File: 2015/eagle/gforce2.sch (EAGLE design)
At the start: 20 parts, among them J1 AVR_SPI_PRG_6PTH, U1 ATMEGA328P_PDIP

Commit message: new schematic
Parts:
- added C3, C4: 22pF, SparkFun-Passives:CAPPTH
- added GO_SWITCH: M02PTH, SparkFun-Connectors:M02PTH
- added GPS: (no value), SparkFun-Connectors:M04PTH
- added I2C_1, I2C_2: (no value), SparkFun-Connectors:I2C_STANDARD
- added Q1: (no value), special:XTAL/S
- added R7: 10K, SparkFun-Passives:RESISTORPTH-1/4W
- added SPI_1, SPI_2: (no value), SparkFun-Connectors:M06SILK_FEMALE_PTH
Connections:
- new net GO: GO_SWITCH.1, R7.2, U1.PD4(XCK/T0)
- new net GPS_RX: GPS.3, U1.PD3(INT1)
- new net GPS_TX: GPS.4, U1.PD2(INT0)
- new net N$2: C3.1, Q1.1, U1.PB6(XTAL1/TOSC1)
- new net N$8: C4.1, Q1.2, U1.PB7(XTAL2/TOSC2)
- net GND: now also C3.2, C4.2, GPS.2, I2C_1.1, I2C_2.1, R7.1, SPI_1.1, SPI_2.1
- net MISO: now also SPI_1.4, SPI_2.4
- net MOSI: now also SPI_1.3, SPI_2.3
- net RX: now also U1.PD0(RXD)
- net SCK: now also SPI_1.5, SPI_2.5
- net SCL: now also I2C_1.4, I2C_2.4
- net SDA: now also I2C_1.3, I2C_2.3
- net SS1: now also SPI_1.6
- net SS2: now also SPI_2.6
- net TX: now also U1.PD1(TXD)
- net VCC: now also GO_SWITCH.2, GPS.1, I2C_1.2, I2C_2.2, SPI_1.2, SPI_2.2

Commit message: new schematic
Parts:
- removed FRAME1: FRAME-LETTER, SparkFun-Aesthetics:FRAME-LETTER
- C2: value (none) -> 0.1uF
- R6: value (none) -> 10K
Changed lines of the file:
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@@
 <part name="GND3" library="SparkFun-Aesthetics" deviceset="GND" device=""/>
 <part name="C1" library="SparkFun-Capacitors" deviceset="CAP" device="PTH" value="0.1uF"/>
-<part name="FRAME1" library="SparkFun-Aesthetics" deviceset="FRAME-LETTER" device=""/>
 <part name="U1" library="SparkFun-DigitalIC" deviceset="ATMEGA328P_PDIP" device=""/>
 <part name="J1" library="SparkFun-Connectors" deviceset="AVR_SPI_PRG_6" device="PTH"/>
@@
 <part name="GND10" library="SparkFun-Aesthetics" deviceset="GND" device=""/>
 <part name="SUPPLY8" library="SparkFun-Aesthetics" deviceset="VCC" device=""/>
-<part name="R6" library="SparkFun-Passives" deviceset="RESISTOR" device="PTH-1/4W"/>
-<part name="C2" library="SparkFun-Capacitors" deviceset="CAP" device="PTH"/>
+<part name="R6" library="SparkFun-Passives" deviceset="RESISTOR" device="PTH-1/4W" value="10K"/>
+<part name="C2" library="SparkFun-Capacitors" deviceset="CAP" device="PTH" value="0.1uF"/>
 <part name="SUPPLY9" library="SparkFun-Aesthetics" deviceset="VCC" device=""/>
 <part name="MC" library="SparkFun-Connectors" deviceset="M04" device="PTH"/>
@@
 <instance part="GND3" gate="1" x="-10.16" y="76.2"/>
 <instance part="C1" gate="G$1" x="15.24" y="83.82"/>
-<instance part="FRAME1" gate="G$1" x="-35.56" y="-73.66"/>
-<instance part="FRAME1" gate="G$2" x="111.76" y="-73.66"/>
 <instance part="U1" gate="G$1" x="88.9" y="50.8"/>
 <instance part="J1" gate="G$1" x="10.16" y="50.8"/>

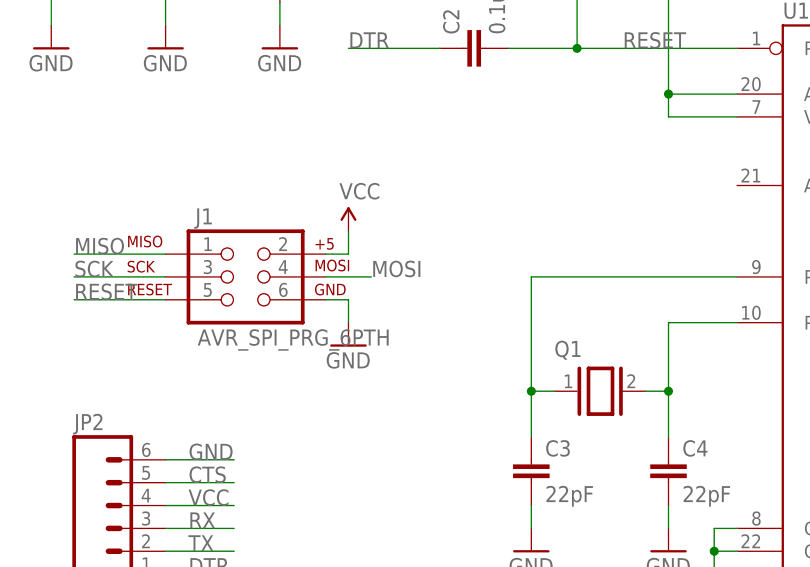
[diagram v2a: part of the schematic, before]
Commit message: version ordered (plus missing pin labels for motor controller)
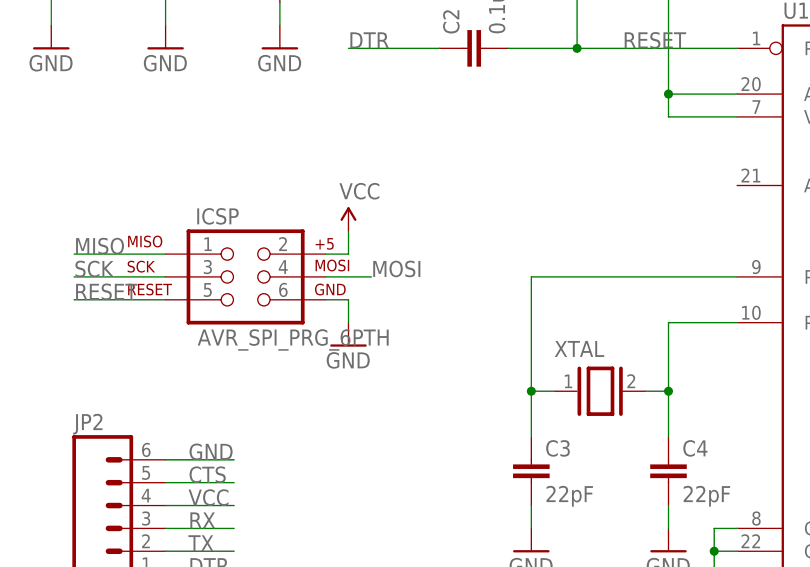
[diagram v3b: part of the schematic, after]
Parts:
- renumbered J1 to ICSP, Q1 to XTAL
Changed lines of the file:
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@@
 <part name="C1" library="SparkFun-Capacitors" deviceset="CAP" device="PTH" value="0.1uF"/>
 <part name="U1" library="SparkFun-DigitalIC" deviceset="ATMEGA328P_PDIP" device=""/>
-<part name="J1" library="SparkFun-Connectors" deviceset="AVR_SPI_PRG_6" device="PTH"/>
+<part name="ICSP" library="SparkFun-Connectors" deviceset="AVR_SPI_PRG_6" device="PTH"/>
 <part name="JP2" library="SparkFun-Connectors" deviceset="M06" device="SILK_FEMALE_PTH"/>
 <part name="SONIC1" library="SparkFun-Connectors" deviceset="M04" device="PTH"/>
@@
 <part name="GND11" library="SparkFun-Aesthetics" deviceset="GND" device=""/>
 <part name="SUPPLY10" library="SparkFun-Aesthetics" deviceset="VCC" device=""/>
-<part name="Q1" library="special" deviceset="XTAL/S" device=""/>
+<part name="XTAL" library="special" deviceset="XTAL/S" device=""/>
 <part name="C3" library="SparkFun-Passives" deviceset="CAP" device="PTH" value="22pF"/>
 <part name="C4" library="SparkFun-Passives" deviceset="CAP" device="PTH" value="22pF"/>
@@
 <instance part="C1" gate="G$1" x="15.24" y="83.82"/>
 <instance part="U1" gate="G$1" x="88.9" y="50.8"/>
-<instance part="J1" gate="G$1" x="10.16" y="50.8"/>
+<instance part="ICSP" gate="G$1" x="10.16" y="50.8"/>
 <instance part="JP2" gate="G$1" x="-2.54" y="22.86"/>
 <instance part="SONIC1" gate="G$1" x="170.18" y="86.36"/>
@@
 <instance part="GND11" gate="1" x="121.92" y="-30.48"/>
 <instance part="SUPPLY10" gate="G$1" x="121.92" y="-5.08"/>
-<instance part="Q1" gate="G$1" x="50.8" y="38.1"/>
+<instance part="XTAL" gate="G$1" x="50.8" y="38.1"/>
 <instance part="C3" gate="G$1" x="43.18" y="27.94"/>
 <instance part="C4" gate="G$1" x="58.42" y="27.94"/>
@@
 </segment>
 <segment>
-<pinref part="J1" gate="G$1" pin="6"/>
+<pinref part="ICSP" gate="G$1" pin="6"/>
 <wire x1="20.32" y1="48.26" x2="22.86" y2="48.26" width="0.1524" layer="91"/>
 <pinref part="GND9" gate="1" pin="GND"/>
@@
 </segment>
 <segment>
-<pinref part="J1" gate="G$1" pin="2"/>
+<pinref part="ICSP" gate="G$1" pin="2"/>
 <wire x1="20.32" y1="53.34" x2="22.86" y2="53.34" width="0.1524" layer="91"/>
 <pinref part="SUPPLY7" gate="G$1" pin="VCC"/>
@@
 <net name="MOSI" class="0">
 <segment>
-<pinref part="J1" gate="G$1" pin="4"/>
+<pinref part="ICSP" gate="G$1" pin="4"/>
 <wire x1="20.32" y1="50.8" x2="25.4" y2="50.8" width="0.1524" layer="91"/>
 <label x="25.4" y="50.8" size="1.778" layer="95"/>
@@
 <net name="MISO" class="0">
 <segment>
-<pinref part="J1" gate="G$1" pin="1"/>
+<pinref part="ICSP" gate="G$1" pin="1"/>
 <wire x1="2.54" y1="53.34" x2="-7.62" y2="53.34" width="0.1524" layer="91"/>
 <label x="-7.62" y="53.34" size="1.778" layer="95"/>
@@
 <net name="SCK" class="0">
 <segment>
-<pinref part="J1" gate="G$1" pin="3"/>
+<pinref part="ICSP" gate="G$1" pin="3"/>
 <wire x1="2.54" y1="50.8" x2="-7.62" y2="50.8" width="0.1524" layer="91"/>
 <label x="-7.62" y="50.8" size="1.778" layer="95"/>
@@
 <net name="RESET" class="0">
 <segment>
-<pinref part="J1" gate="G$1" pin="5"/>
+<pinref part="ICSP" gate="G$1" pin="5"/>
 <wire x1="2.54" y1="48.26" x2="-7.62" y2="48.26" width="0.1524" layer="91"/>
 <label x="-7.62" y="48.26" size="1.778" layer="95"/>
@@
 <wire x1="66.04" y1="50.8" x2="43.18" y2="50.8" width="0.1524" layer="91"/>
 <wire x1="43.18" y1="50.8" x2="43.18" y2="38.1" width="0.1524" layer="91"/>
-<pinref part="Q1" gate="G$1" pin="1"/>
+<pinref part="XTAL" gate="G$1" pin="1"/>
 <wire x1="43.18" y1="38.1" x2="45.72" y2="38.1" width="0.1524" layer="91"/>
 <junction x="43.18" y="38.1"/>
@@
 <wire x1="66.04" y1="45.72" x2="58.42" y2="45.72" width="0.1524" layer="91"/>
 <wire x1="58.42" y1="45.72" x2="58.42" y2="38.1" width="0.1524" layer="91"/>
-<pinref part="Q1" gate="G$1" pin="2"/>
+<pinref part="XTAL" gate="G$1" pin="2"/>
 <wire x1="58.42" y1="38.1" x2="55.88" y2="38.1" width="0.1524" layer="91"/>
 <junction x="58.42" y="38.1"/>
